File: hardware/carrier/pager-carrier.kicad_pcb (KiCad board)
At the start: 2 copper layers, 46.2 x 51 mm, 89 parts, among them J1 PANEL, J2 CARDKB, J3 HAPTIC, J4 EXT_LED, J5 PIEZ, J6 USB4235, J7 BATTERY, M1 Walter, Q1 UMH3N, Q2 SI1308EDL, Q3 MMST3904, Q4 AO3401A, SW1 KMR221GLFS, SW2 JS102011SAQN, U1 CP2102N-A02-GQFN24, U2 SN74LVC2G126DCUR, U3 DRV2605LDGSR, U4 LIS2DW12TR, U5 BQ25185DLHR, U6 MAX17048G+T10, U7 TPS62840DLCR

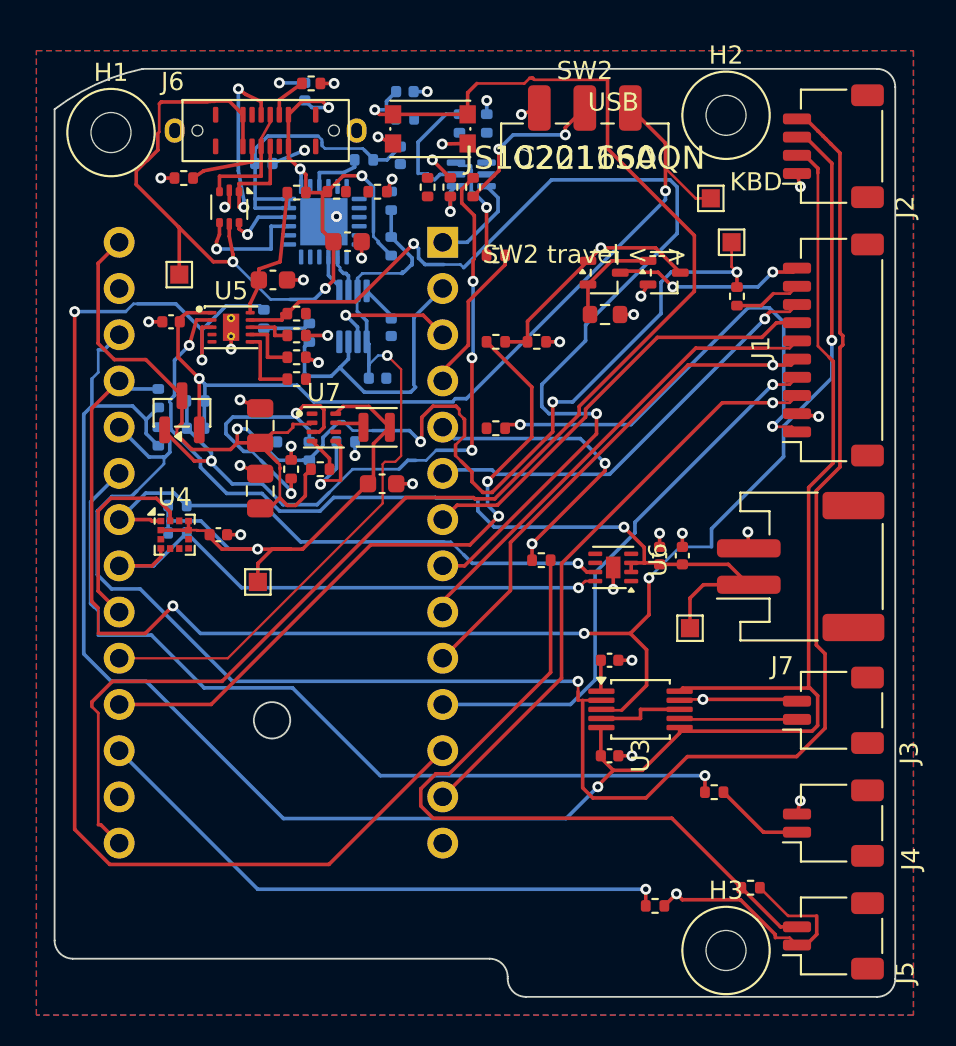
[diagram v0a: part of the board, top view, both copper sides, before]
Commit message: Carrier: top-biased re-route (via cost 20, B.Cu trace cost x2.2), Freerouting variant 17 (15 open signal links, was 18)
Six trials with Freerouting biased toward F.Cu and cheaper vias (pre-route base rebuilt from
the owner's board, so the test points and the hand-routed VBUS_DET are kept
as fixed items). Best variant installed; 0 DRC errors; remaining open links
are listed in HANDOFF-v0.2.md for hand finishing. STEP re-exported.

Co-Authored-By: Claude Fable 5.1 <noreply@anthropic.com>
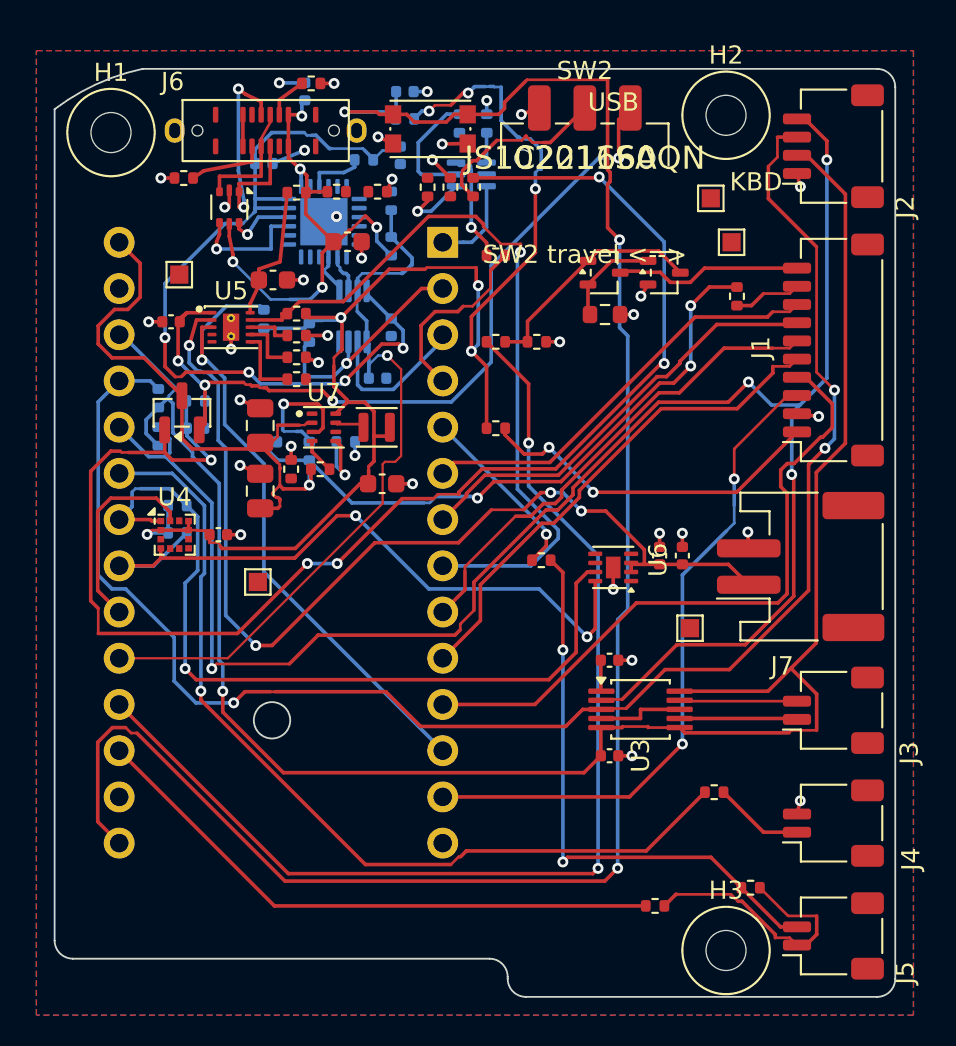
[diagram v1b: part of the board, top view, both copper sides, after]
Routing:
- net 3V3: track 34.0 -> 78.5 mm, vias 1 -> 7
- net Net-(Q4-G): track 39.4 -> 77.4 mm, vias 4 -> 5
- net CHG_STAT2: track 67.9 -> 35.1 mm, vias 2 -> 1
- net /Core/BRG_3V3: track 18.8 -> 46.2 mm, vias 0 -> 4
- net /Core/FL_PWM: track 37.0 -> 61.8 mm
- net VBUS: track 53.8 -> 29.6 mm
- net /Core/FL_BTN: track 81.9 -> 103.2 mm, vias 1 -> 3
- net CHG_STAT1: track 59.3 -> 42.3 mm, vias 2 -> 1
- net AON_SCL: track 30.9 -> 44.6 mm
- net 3V3_AWK: track 114.1 -> 104.6 mm
- net SYS_SW: track 77.0 -> 68.0 mm
- net Net-(J5-Pin_2): track 40.3 -> 31.4 mm, vias 0 -> 2
- net Net-(U7-MODE): track 15.8 -> 7.28 mm, vias 2 -> 1
- net /Core/PIEZ_N: track 16.7 -> 9.99 mm, vias 2 -> 1
- net AON_SDA: track 31.3 -> 37.9 mm, vias 1 -> 2
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
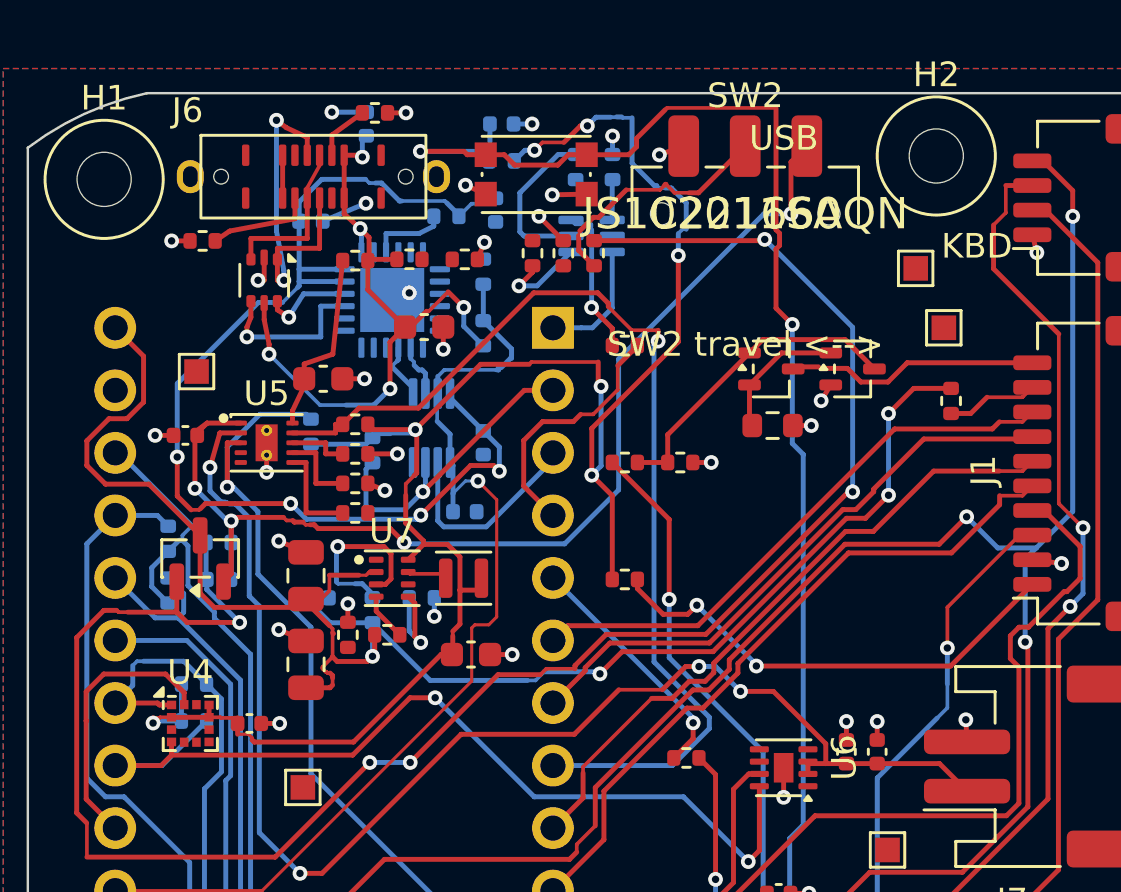
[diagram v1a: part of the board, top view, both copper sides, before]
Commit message: Carrier: prune redundant GND vias (pads already on the pour), morning summary in the handoff
Each GND via with only short stubs to pads that the pour already touches was
removed one at a time and kept only if the connectivity count did not grow.
DRC 0 errors; open links unchanged.

Co-Authored-By: Claude Fable 5.1 <noreply@anthropic.com>
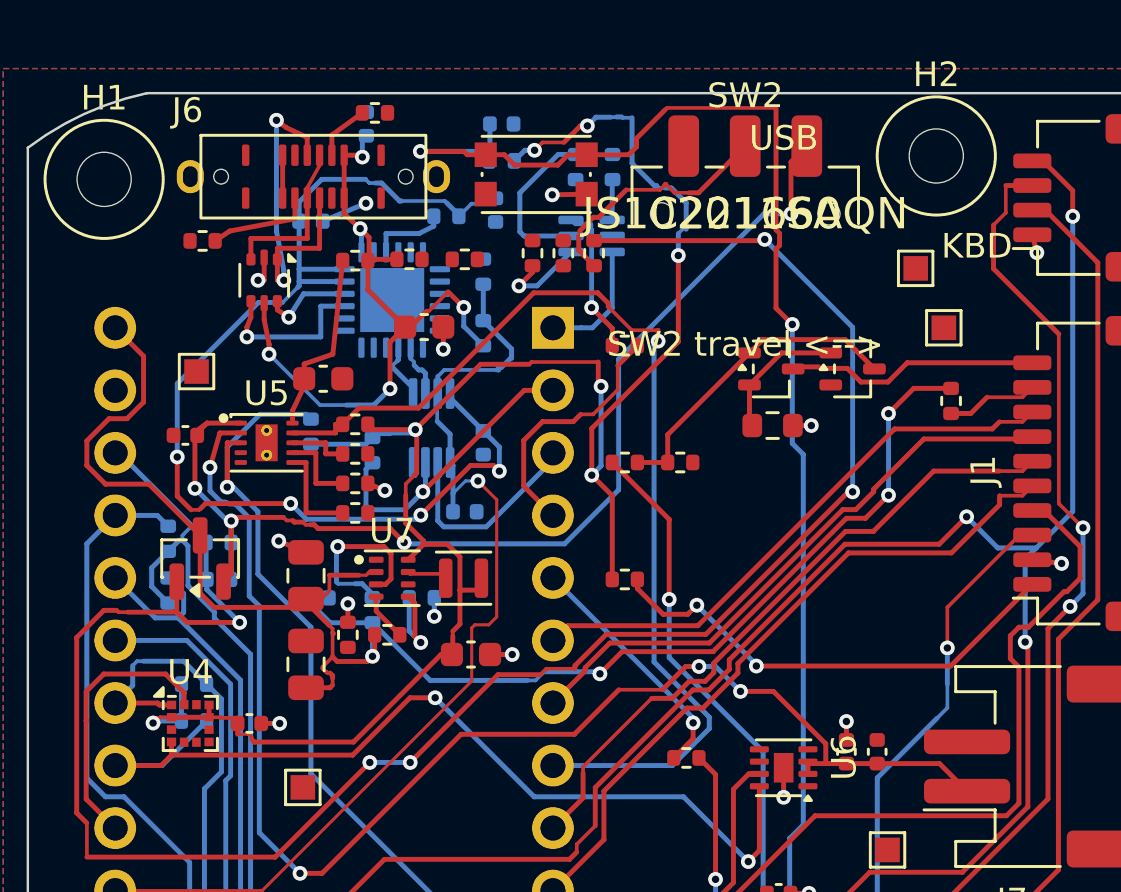
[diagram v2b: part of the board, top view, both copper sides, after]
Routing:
- net GND: track 39.8 -> 22.2 mm, vias 37 -> 18

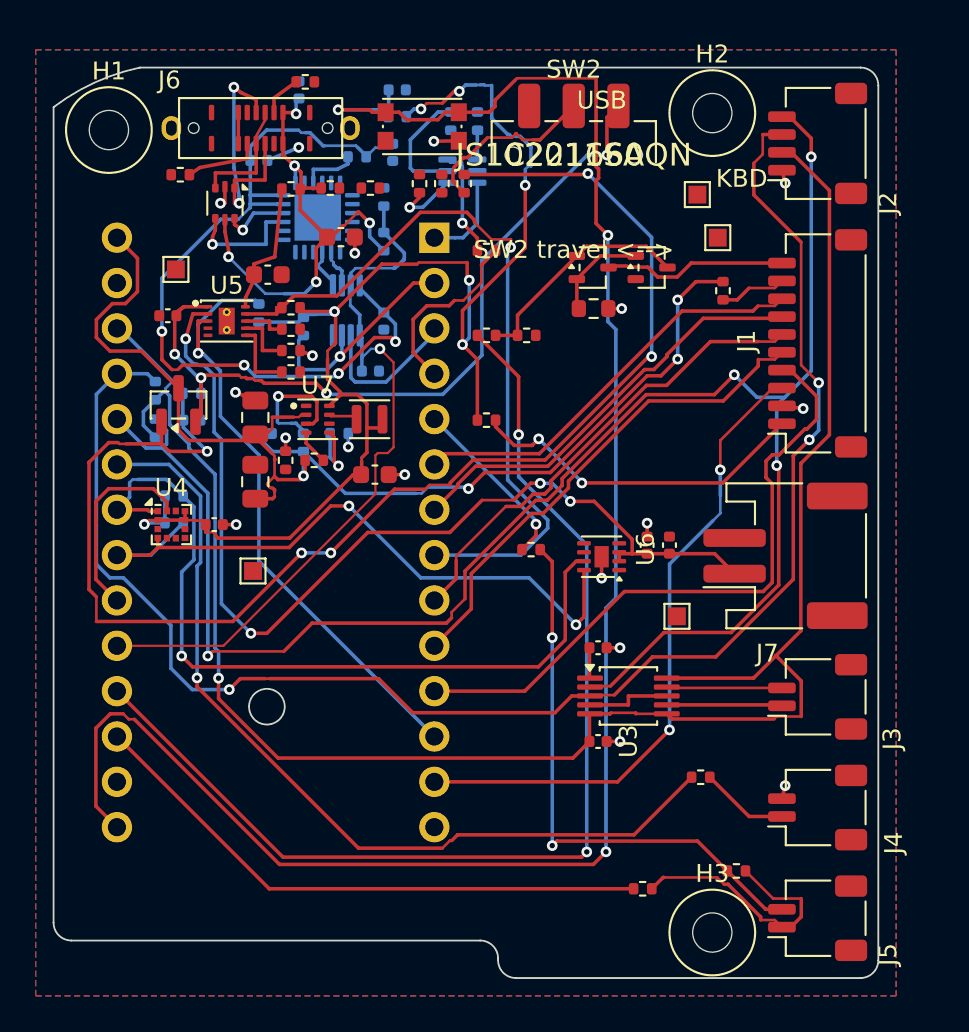
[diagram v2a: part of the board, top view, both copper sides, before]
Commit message: Carrier: grid-repair the test-point links the router skipped, stitch pour islands (unconnected 20 -> 9)
The routing copy still detached test-point pads (a rule from when they were
parked off-board), so TP7-TP11 were never routed; pipeline fixed, the links
closed with the grid repair, a zero-length stub cleaned, pour islands
stitched. DRC 0 errors.

Co-Authored-By: Claude Fable 5.1 <noreply@anthropic.com>
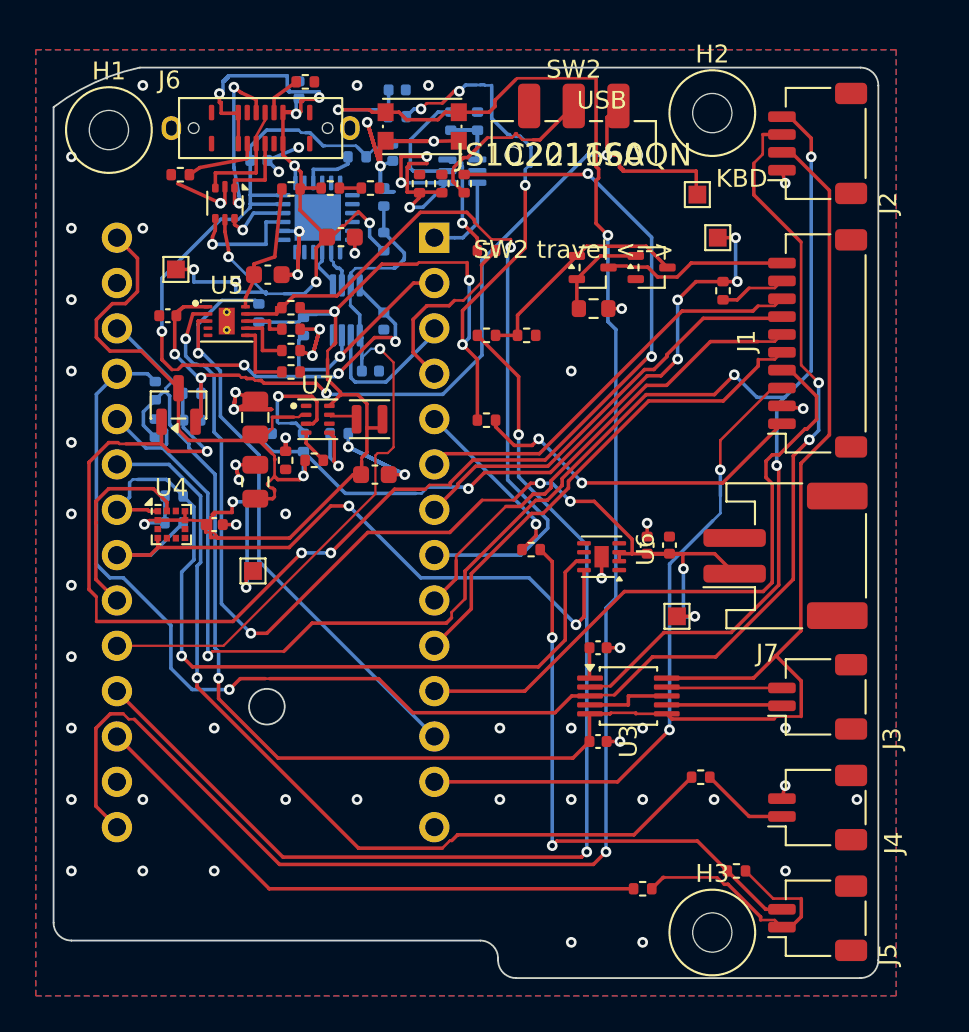
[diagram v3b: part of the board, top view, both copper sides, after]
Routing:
- net GND: track 22.2 -> 115.9 mm, vias 18 -> 62
- net VBUS: track 29.6 -> 49.2 mm, vias 5 -> 9
- net 3V3: track 78.5 -> 89.2 mm, vias 7 -> 9
- net Net-(Q1A-E1): track 3.73 -> 14.3 mm, vias 1 -> 3
- net SYS: track 46.8 -> 54.1 mm
- net VBAT: track 55.0 -> 62.2 mm, vias 4 -> 6
- net Net-(Q1B-E2): track 1.65 -> 6.29 mm
- net SYS_SW: track 68.0 -> 72.5 mm, vias 4 -> 6
- net Net-(U1-VBUS): track 0.00 -> 1.23 mm

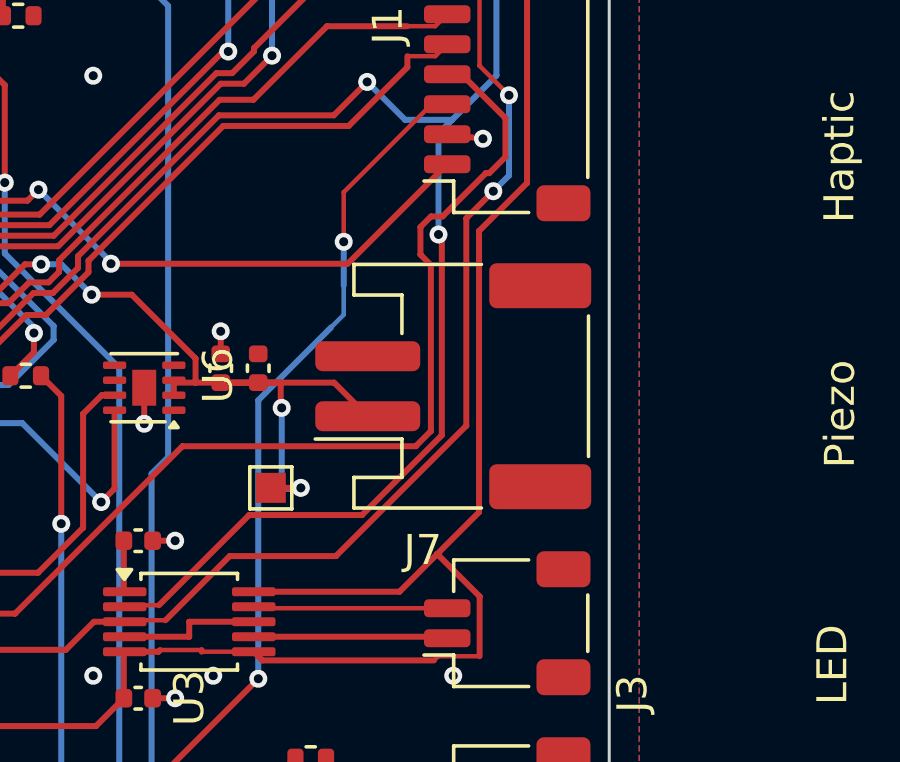
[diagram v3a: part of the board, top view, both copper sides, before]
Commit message: Carrier: battery connector J7 -> JST SH SM02B-SRSS-TB (LCSC C160402)
Replaces the 5.5 mm JST PH S2B-PH-SM4-TB, which sat above the display glass back.
SH side-entry is 2.9 mm tall and matches J3/J4/J5. Schematic fields, board footprint
(KiCad library model), VBAT stub re-hooked, pours refilled. ERC 0, DRC 0 errors,
9 unconnected (unchanged). STEP re-exported. Handoff notes the J2 MPN/footprint mismatch.

Co-Authored-By: Claude Fable 5.1 <noreply@anthropic.com>
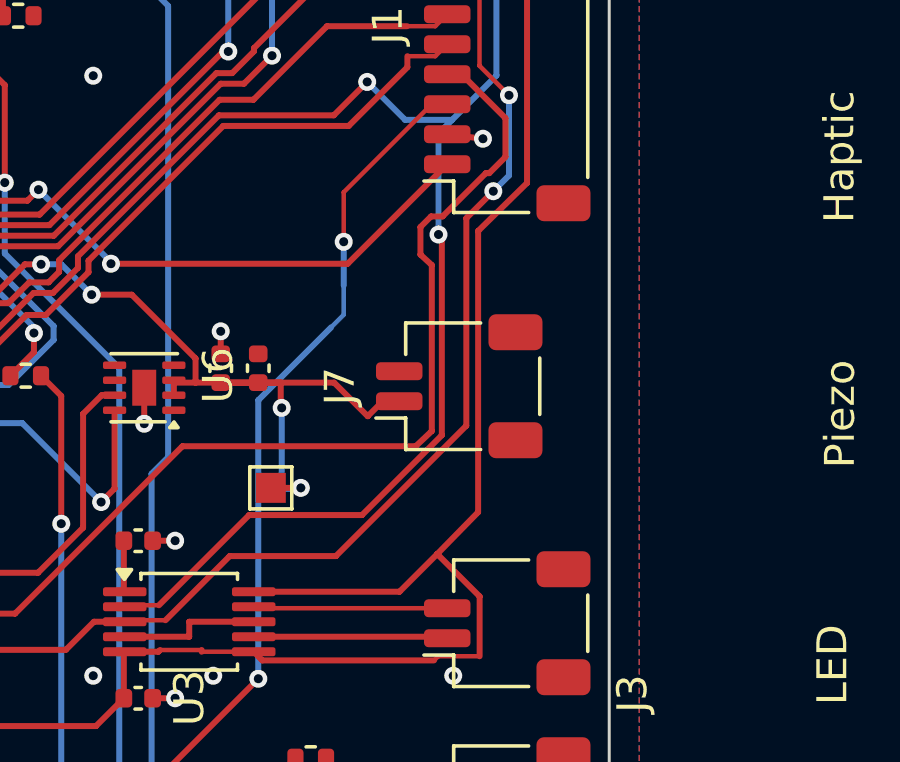
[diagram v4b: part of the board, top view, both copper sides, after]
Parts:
- J7: footprint Connector_JST:JST_PH_S2B-PH-SM4-TB_1x02-1MP_P2.00mm_Horizontal -> Connector_JST:JST_SH_SM02B-SRSS-TB_1x02-1MP_P1.00mm_Horizontal
- moved J7 0.20 mm to (115.5, 84.8)
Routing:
- net VBAT: track 62.2 -> 63.4 mm
